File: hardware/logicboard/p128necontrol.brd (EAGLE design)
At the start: 95 x 72 mm, 32 parts, among them IC1 74LS595N, IC2 74LS595N, IC3 74LS595N, IC4 74LS595N, IC5 74LS595N, IC6 74LS595N, IC7 74LS595N, IC8 74LS595N

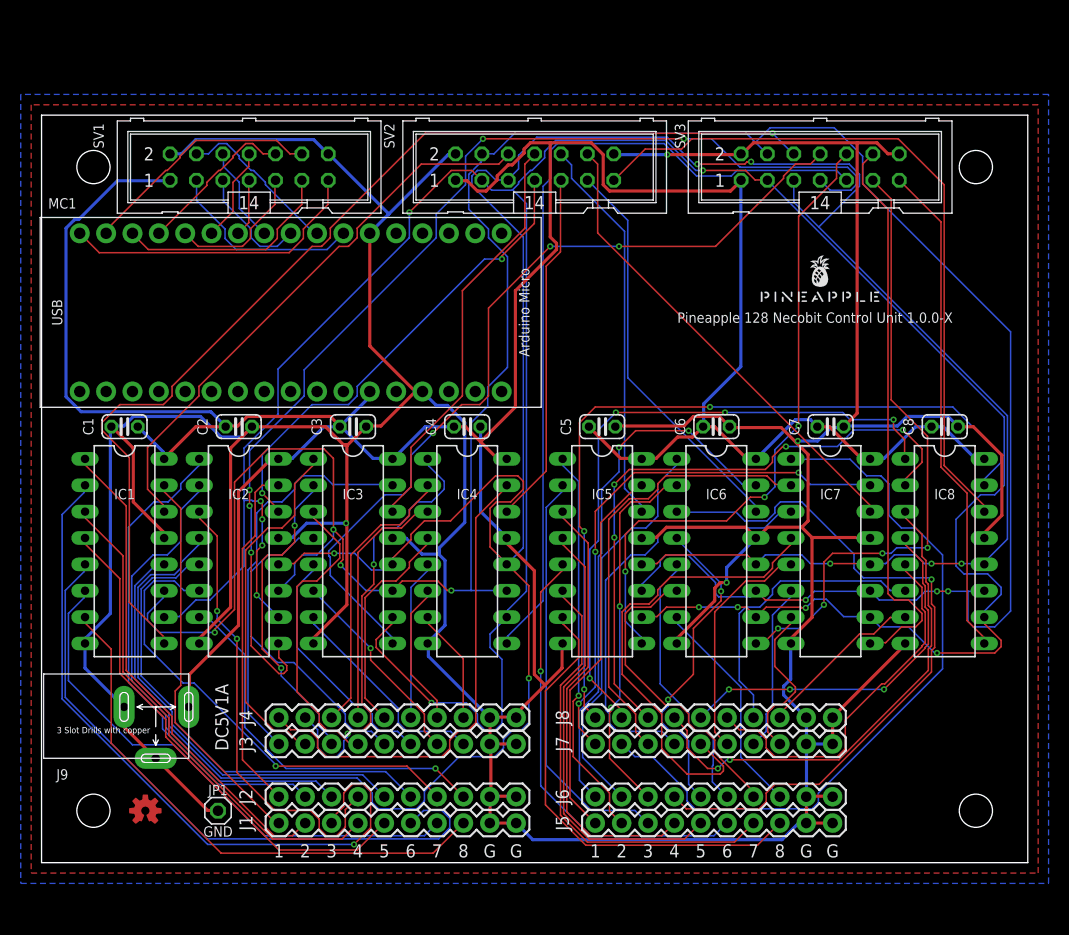
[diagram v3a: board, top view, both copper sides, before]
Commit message: Now necontroler (Necobit Controler) has LED indicator.
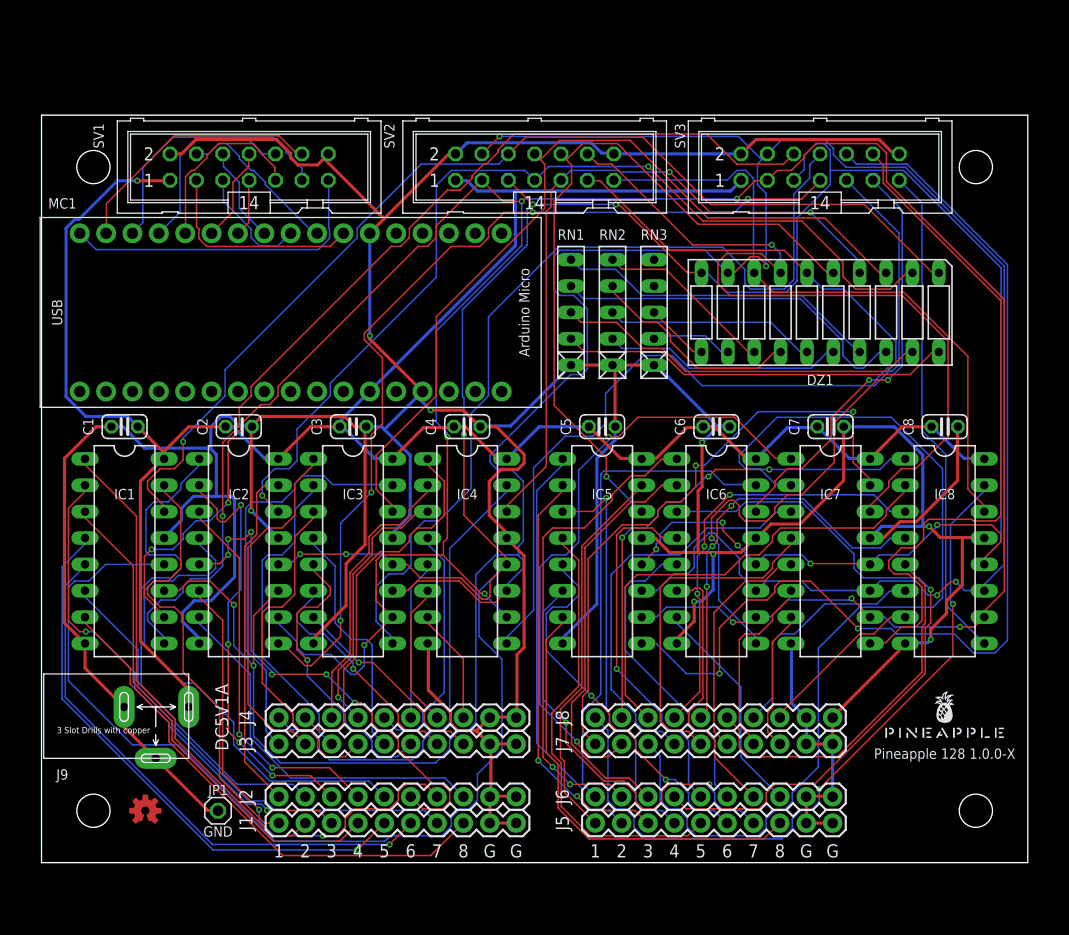
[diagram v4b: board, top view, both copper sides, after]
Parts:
- added DZ1: LB10, led:LB10
- added RN1, RN2, RN3: 160, resistor-net:RN-5
- J9: value (none) -> DC5V
- moved U$1 43.7 mm to (87.0, 12.0)
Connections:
- new net N$1: DZ1.20, RN1.2
- new net N$10: DZ1.11, RN3.3
- new net N$2: DZ1.19, RN1.3
- new net N$3: DZ1.18, RN1.4
- new net N$4: DZ1.17, RN1.5
- new net N$5: DZ1.16, RN2.2
- new net N$6: DZ1.15, RN2.3
- new net N$7: DZ1.14, RN2.4
- new net N$8: DZ1.13, RN2.5
- new net N$9: DZ1.12, RN3.2
- net GND: now also RN1.1, RN2.1, RN3.1
- net RCLK: now also DZ1.10
- net SCLK: now also DZ1.9
- net SIN1: now also DZ1.1
- net SIN2: now also DZ1.2
- net SIN3: now also DZ1.3
- net SIN4: now also DZ1.4
- net SIN5: now also DZ1.5
- net SIN6: now also DZ1.6
- net SIN7: now also DZ1.7
- net SIN8: now also DZ1.8
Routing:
- net N703: track 43.2 -> 94.4 mm
- net SIN1: track 54.4 -> 102.3 mm, vias 0 -> 1
- net SIN2: track 46.5 -> 93.5 mm
- net VCC: track 267.0 -> 222.3 mm, vias 0 -> 1
- net SIN3: track 40.1 -> 81.7 mm
- net XOUT5: track 62.4 -> 102.5 mm, vias 3 -> 2
- net N$1: track 0.00 -> 37.8 mm
- net SCLK: track 258.0 -> 294.2 mm, vias 7 -> 6
- net N$2: track 0.00 -> 36.0 mm
- net N$3: track 0.00 -> 35.1 mm
- net SIN4: track 34.1 -> 68.0 mm, vias 0 -> 2
- net SIN5: track 37.7 -> 70.6 mm, vias 0 -> 1
- net SIN7: track 45.7 -> 78.5 mm, vias 0 -> 1
- net N$4: track 0.00 -> 31.5 mm
- net N$5: track 0.00 -> 23.1 mm
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- removed copper zone on layer 1, net GND
- removed copper zone on layer 16, net GND
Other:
- board text added: "Pineapple 128 1.0.0-X"
- board text removed: "Pineapple 128 Necobit Control Unit 1.0.0-X"
